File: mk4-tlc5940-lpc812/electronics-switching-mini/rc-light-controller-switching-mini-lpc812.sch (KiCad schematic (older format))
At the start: 12 parts, among them J1 Conn_01x03, J2 Pinheader straight 1x06, J3 Pinheader straight 1x06, T1 PMV30UN, T2 PMV30UN, T3 PMV30UN, U1 LPC812M101JDH20, U2 MCP1703A-3302_SOT23

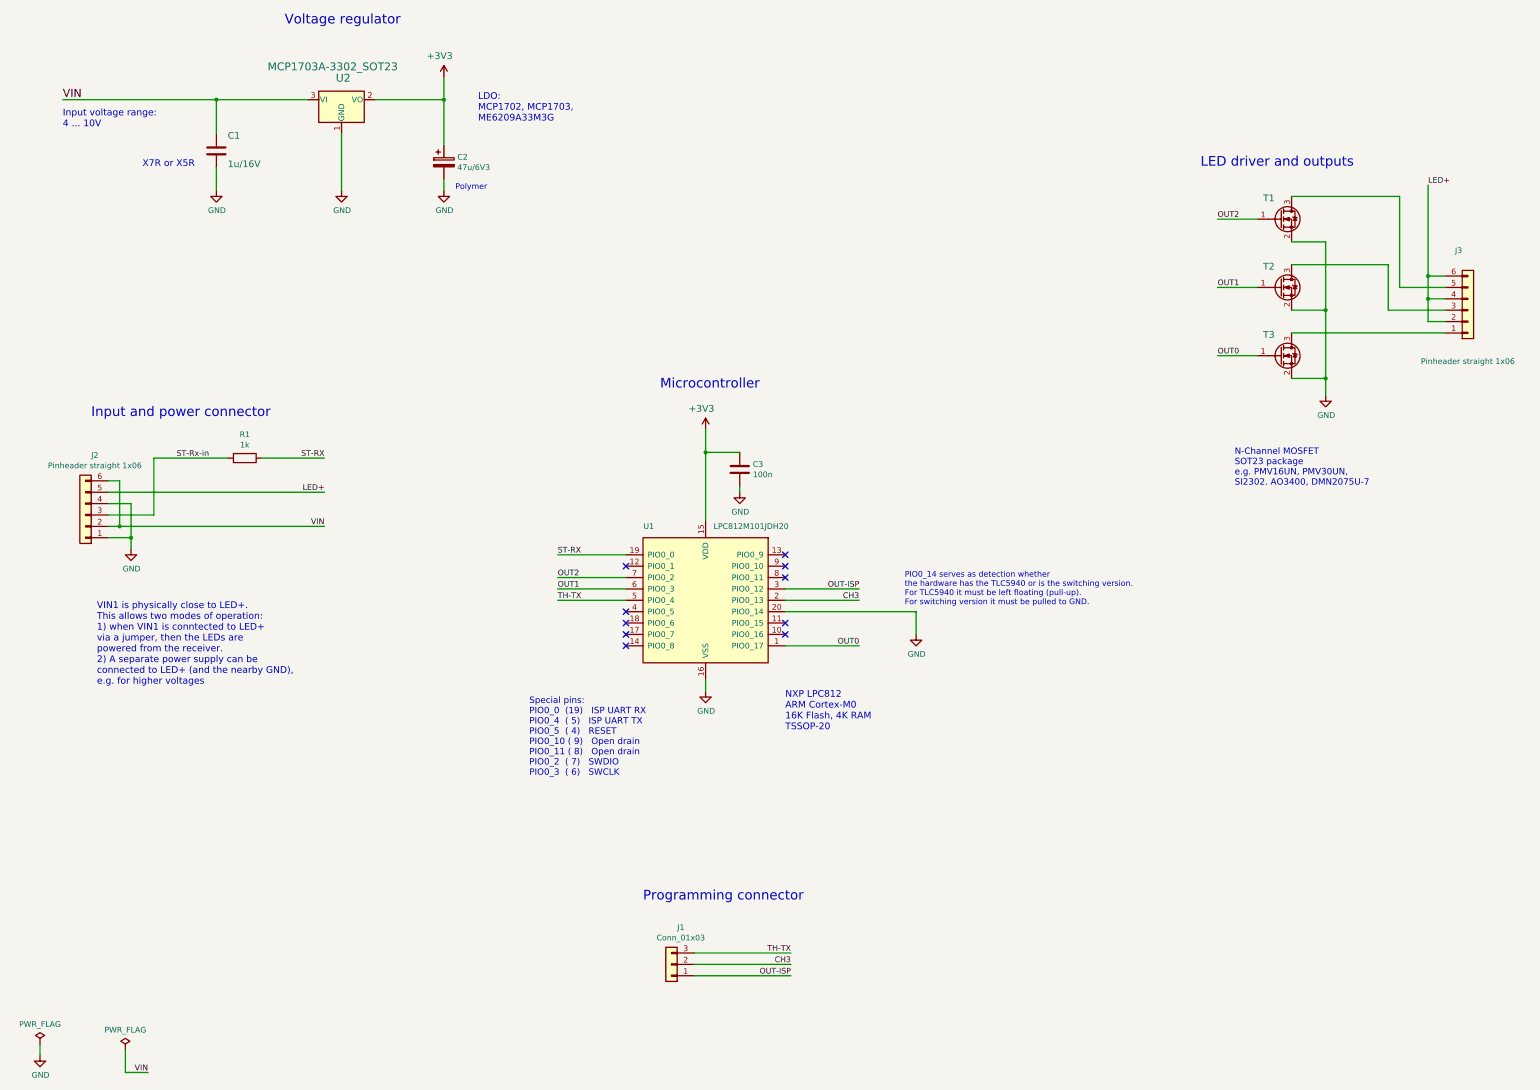
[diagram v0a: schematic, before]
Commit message: Add resistor networ to protect TH-Tx/CH3/OUT-ISP
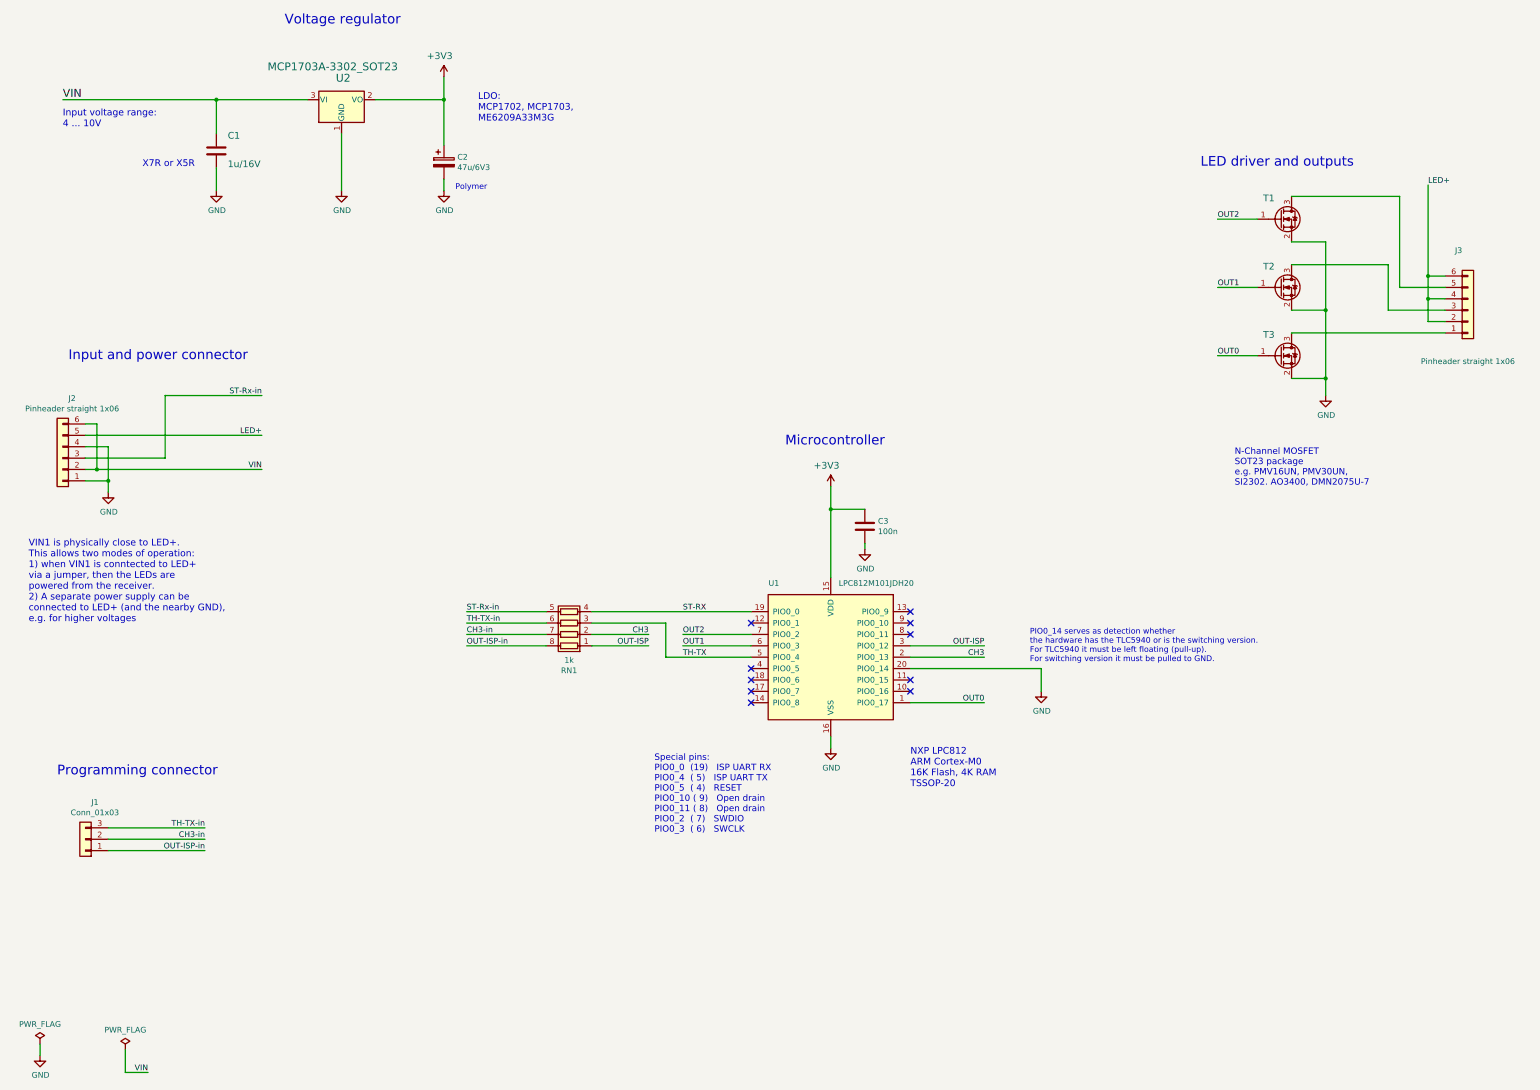
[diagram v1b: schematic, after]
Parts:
- removed R1: 1k, Resistor_SMD:R_0603_1608Metric_Pad0.98x0.95mm_HandSolder, symbol Device:R
- added RN1: 1k, Resistor_SMD:R_Array_Convex_4x0603, symbol Device:R_Pack04
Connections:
- net CH3: now also RN1.2 (R2.1); no longer J1.2 (Pin_2)
- net OUT-ISP: now also RN1.1 (R1.1); no longer J1.1 (Pin_1)
- net ST-RX: now also RN1.4 (R4.1)
- net ST-Rx-in: now also RN1.5 (R4.2)
- net TH-TX: now also RN1.3 (R3.1); no longer J1.3 (Pin_3)
- new net CH3-in: J1.2 (Pin_2), RN1.7 (R2.2)
- new net OUT-ISP-in: J1.1 (Pin_1), RN1.8 (R1.2)
- new net TH-TX-in: J1.3 (Pin_3), RN1.6 (R3.2)
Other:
- moved on the sheet: C3, J1, J2, U1
